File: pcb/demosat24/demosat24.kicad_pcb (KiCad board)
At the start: 2 copper layers, 68.6 x 53.3 mm, 11 parts, among them J1 Power, J2 Digital/PWM, J3 Analog, J4 Digital/PWM, J5 Conn_01x04, J6 Conn_01x04, J7 Conn_01x02

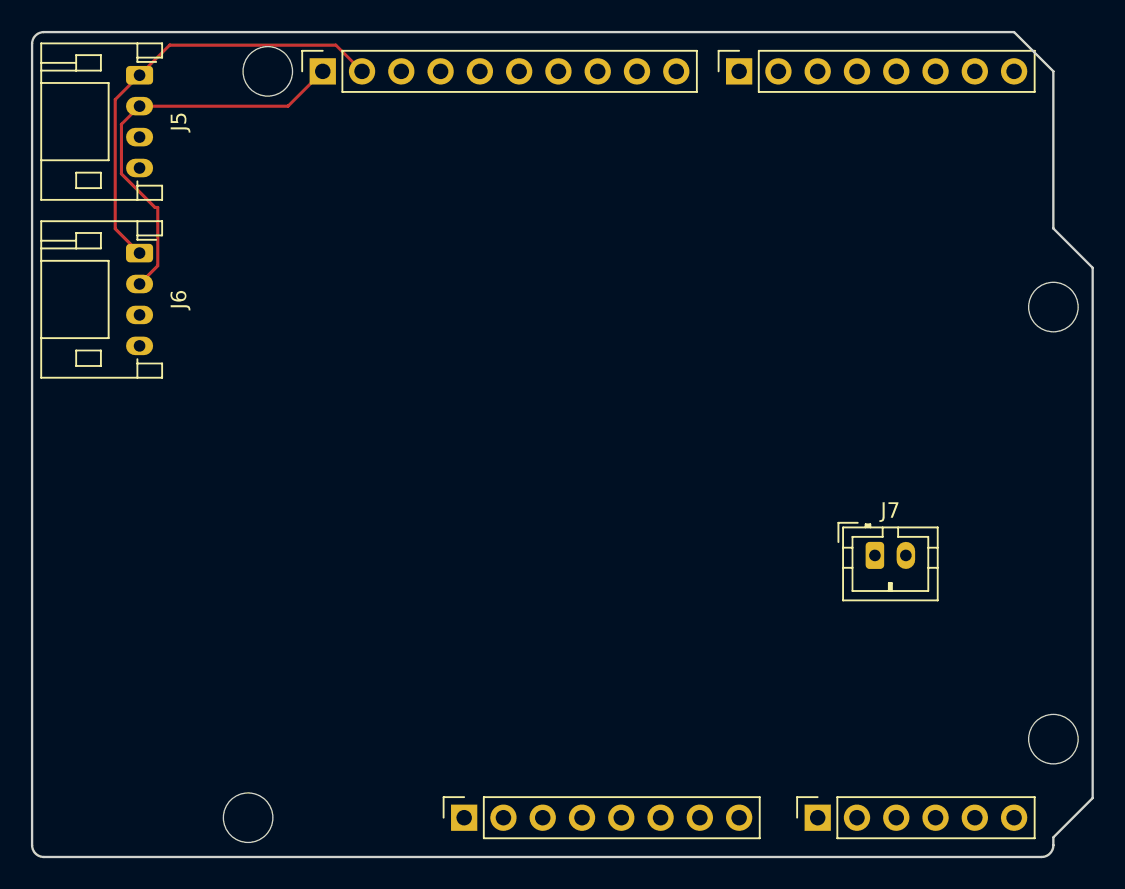
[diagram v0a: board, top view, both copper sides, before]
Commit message: pcb with one servo, all data and power connected but not ground
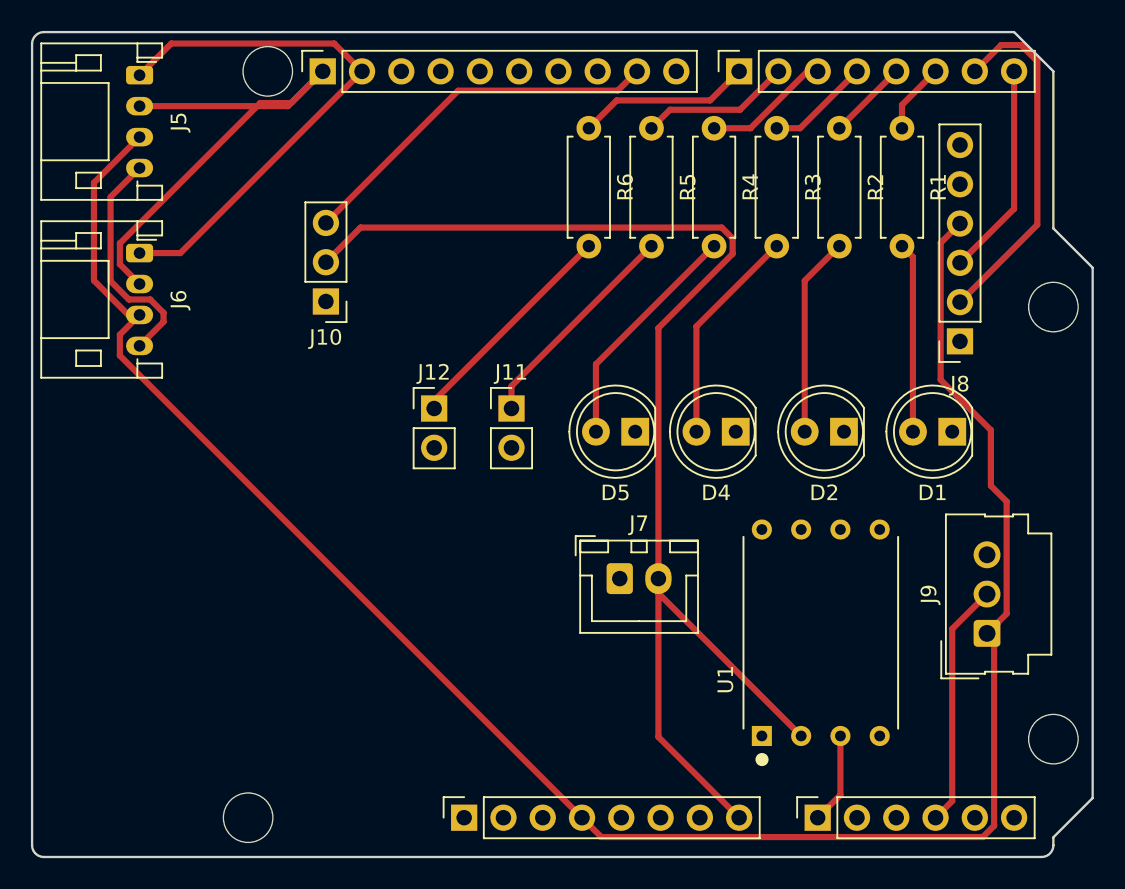
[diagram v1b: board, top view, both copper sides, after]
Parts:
- added D1: LED, LED_THT:LED_D5.0mm, F.Cu at (159.5, 72.5)
- added D2: LED, LED_THT:LED_D5.0mm, F.Cu at (152.5, 72.5)
- added D4: LED, LED_THT:LED_D5.0mm, F.Cu at (145.5, 72.5)
- added D5: LED, LED_THT:LED_D5.0mm, F.Cu at (139.0, 72.5)
- added J10: Conn_01x03, Connector_PinHeader_2.54mm:PinHeader_1x03_P2.54mm_Vertical, F.Cu at (119.0, 64.1)
- added J11: Conn_01x02, Connector_PinHeader_2.54mm:PinHeader_1x02_P2.54mm_Vertical, F.Cu at (131.0, 71.0)
- added J12: Conn_01x02, Connector_PinHeader_2.54mm:PinHeader_1x02_P2.54mm_Vertical, F.Cu at (126.0, 71.0)
- added J8: Conn_01x06, Connector_PinSocket_2.54mm:PinSocket_1x06_P2.54mm_Vertical, F.Cu at (160.0, 66.7)
- added J9: Conn_01x03, Connector_Molex:Molex_SL_171971-0003_1x03_P2.54mm_Vertical, F.Cu at (161.8, 85.5)
- added R1: 220R, Resistor_THT:R_Axial_DIN0207_L6.3mm_D2.5mm_P7.62mm_Horizontal, F.Cu at (156.2, 52.9)
- added R2: 220R, Resistor_THT:R_Axial_DIN0207_L6.3mm_D2.5mm_P7.62mm_Horizontal, F.Cu at (152.2, 52.9)
- added R3: 220R, Resistor_THT:R_Axial_DIN0207_L6.3mm_D2.5mm_P7.62mm_Horizontal, F.Cu at (148.2, 52.9)
- added R4: 220R, Resistor_THT:R_Axial_DIN0207_L6.3mm_D2.5mm_P7.62mm_Horizontal, F.Cu at (144.1, 52.9)
- added R5: 220R, Resistor_THT:R_Axial_DIN0207_L6.3mm_D2.5mm_P7.62mm_Horizontal, F.Cu at (140.1, 52.9)
- added R6: 220R, Resistor_THT:R_Axial_DIN0207_L6.3mm_D2.5mm_P7.62mm_Horizontal, F.Cu at (136.0, 52.9)
- added U1: SSCDANN150PGAA5, libs:XDCR_SSCDANN150PGAA5, F.Cu at (151.0, 85.5)
- J7: footprint Connector_JST:JST_PH_B2B-PH-K_1x02_P2.00mm_Vertical -> Connector_JST:JST_XH_B2B-XH-A_1x02_P2.50mm_Vertical
- moved J7 16.6 mm to (138.0, 82.0)
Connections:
- J5 pad 3: VCC -> +3V3
- J6 pad 3: VCC -> +3V3
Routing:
- net +3V3: track 0.00 -> 129.2 mm
- net VCC: track 0.00 -> 83.1 mm
- net /*9: track 0.00 -> 24.2 mm
- net /TX/1: track 0.00 -> 22.8 mm
- net /A3: track 0.00 -> 15.8 mm
- net Net-(D5-A): track 0.00 -> 15.2 mm
- net GND: track 0.00 -> 15.1 mm
- net Net-(J12-Pin_1): track 0.00 -> 14.6 mm
- net Net-(J11-Pin_1): track 0.00 -> 14.2 mm
- net Net-(D4-A): track 0.00 -> 14.1 mm
- net /RX/0: track 0.00 -> 13.8 mm
- net Net-(D2-A): track 0.00 -> 12.9 mm
- net Net-(D1-A): track 0.00 -> 12.3 mm
- net /7: track 0.00 -> 11.2 mm
- net /*6: track 0.00 -> 9.73 mm
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
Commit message: minor changes to pcb
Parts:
- J7: footprint Connector_JST:JST_XH_B2B-XH-A_1x02_P2.50mm_Vertical -> Connector_JST:JST_PH_B2B-PH-K_1x02_P2.00mm_Vertical
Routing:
- net GND: track 15.1 -> 300.3 mm
- net +3V3: track 129.2 -> 131.1 mm
- net Net-(J12-Pin_1): track 14.6 -> 14.1 mm
